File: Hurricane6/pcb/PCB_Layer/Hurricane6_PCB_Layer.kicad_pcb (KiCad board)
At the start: 2 copper layers, 61.5 x 42.5 mm, 19 parts, among them SW1 SW_1, SW2 SW_2, SW3 SW_3, SW4 SW_4, SW5 SW_5, SW6 SW_6, U1 ProMicro-NoSilk

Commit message: feat: consistency of wiring
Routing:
- net Net-(LED1-Pad2): track 33.8 -> 40.6 mm
- net VCC: track 117.3 -> 114.4 mm
- net Net-(LED3-Pad2): track 35.6 -> 38.4 mm
- net Row0: track 69.5 -> 71.0 mm
- net Col2: track 18.9 -> 20.3 mm
- net Col1: track 13.0 -> 13.5 mm

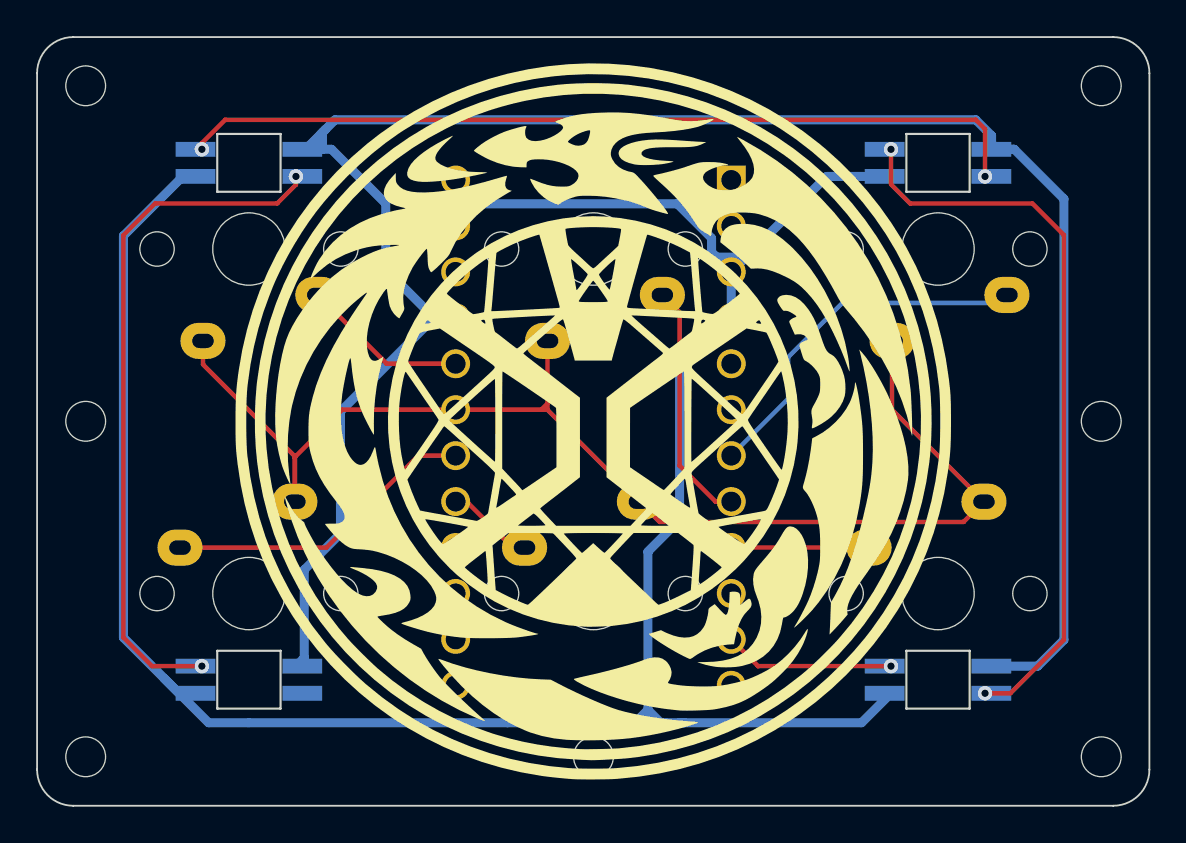
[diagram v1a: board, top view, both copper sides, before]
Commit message: feat: wiring
- consistency of wiring
- remove redundant wiring for GND(pin 3, 23)
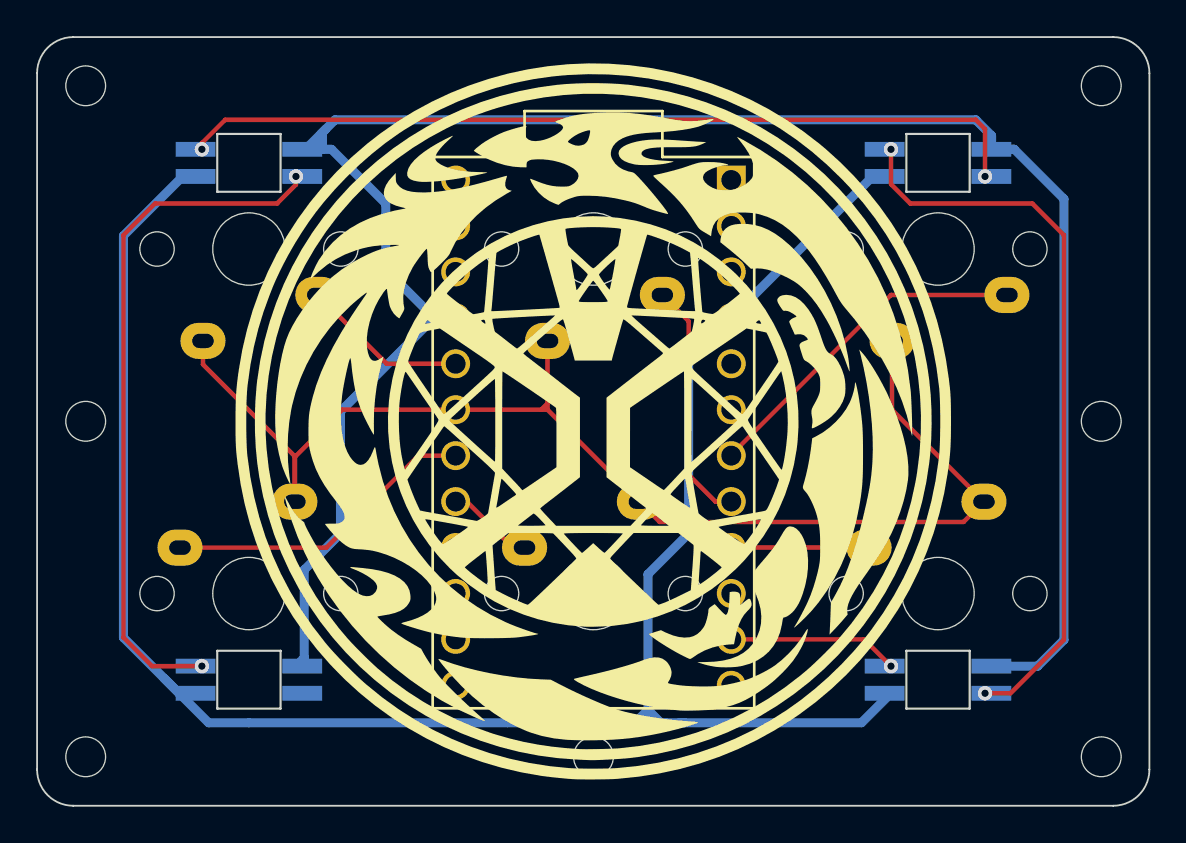
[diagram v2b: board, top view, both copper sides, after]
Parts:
- U1: value ProMicro-NoSilk -> ProMicro; footprint promicro:ProMicro-NoSilk -> promicro:ProMicro
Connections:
- U1 pad 23: GND -> unconnected-(U1-Pad23)
- U1 pad 3: GND -> unconnected-(U1-Pad3)
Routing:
- net GND: track 135.4 -> 114.2 mm
- net Col2: track 20.3 -> 19.6 mm

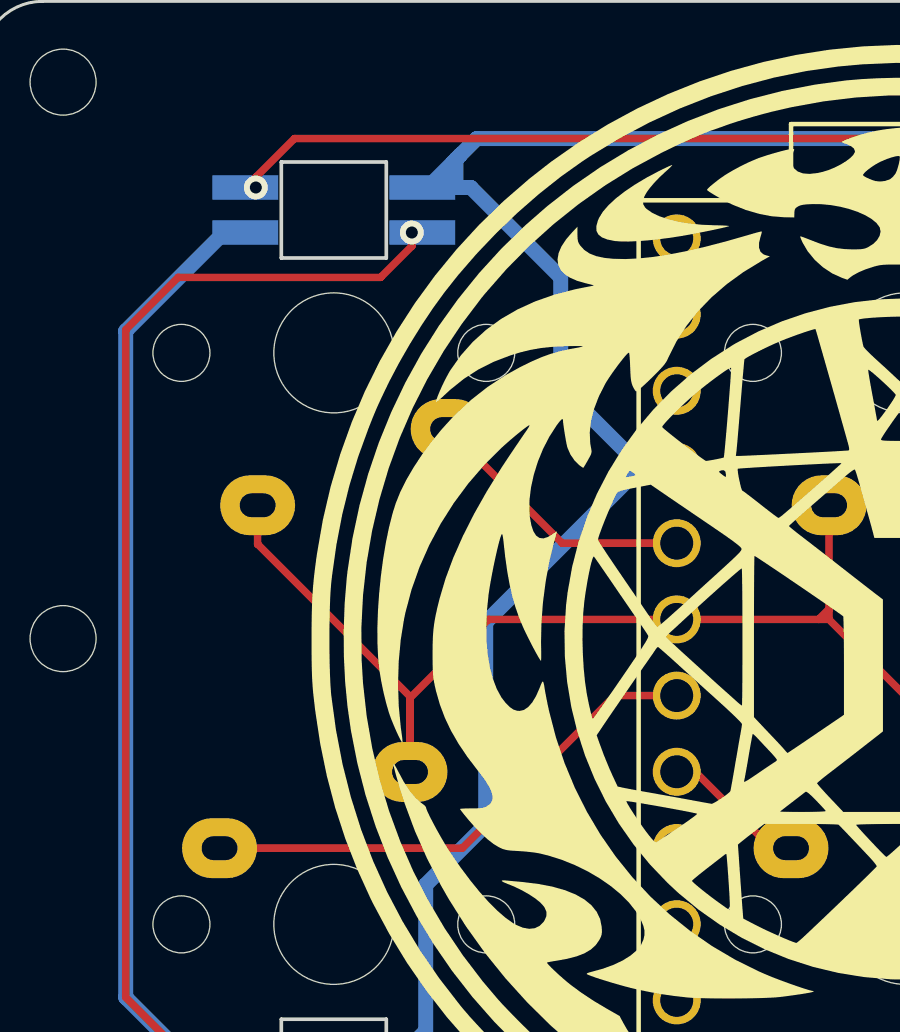
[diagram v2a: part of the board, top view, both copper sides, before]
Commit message: featr: add reset switch and modify wiring
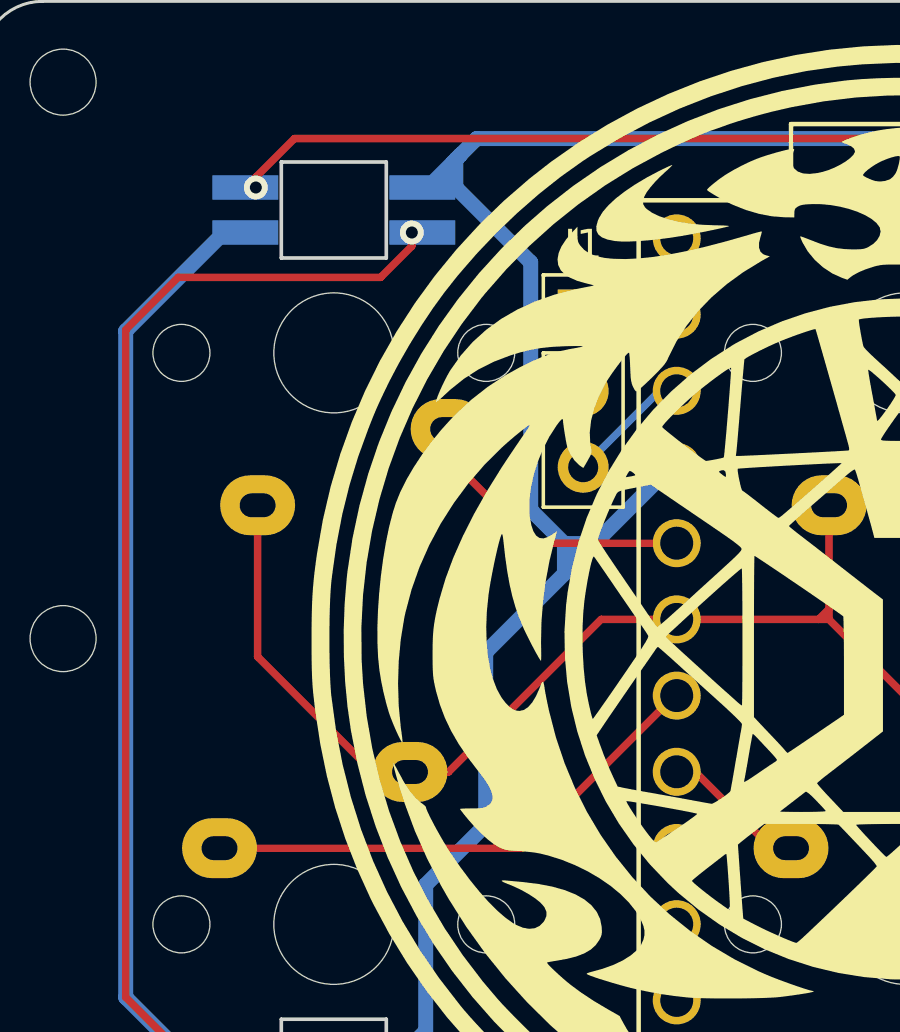
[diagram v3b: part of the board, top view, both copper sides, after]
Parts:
- added J1: Conn_01x03, Connector_PinHeader_2.54mm:PinHeader_1x03_P2.54mm_Vertical, F.Cu at (175.0, 96.2)
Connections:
- U1 pad 22: unconnected-(U1-Pad22) -> Net-(U1-Pad22)
- U1 pad 23: unconnected-(U1-Pad23) -> Net-(U1-Pad23)
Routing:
- net Net-(U1-Pad22): track 0.00 -> 4.20 mm
- net VCC: track 114.4 -> 117.6 mm
- net Net-(U1-Pad23): track 0.00 -> 3.12 mm
- net Row0: track 71.0 -> 70.3 mm
- net Col0: track 9.20 -> 9.75 mm

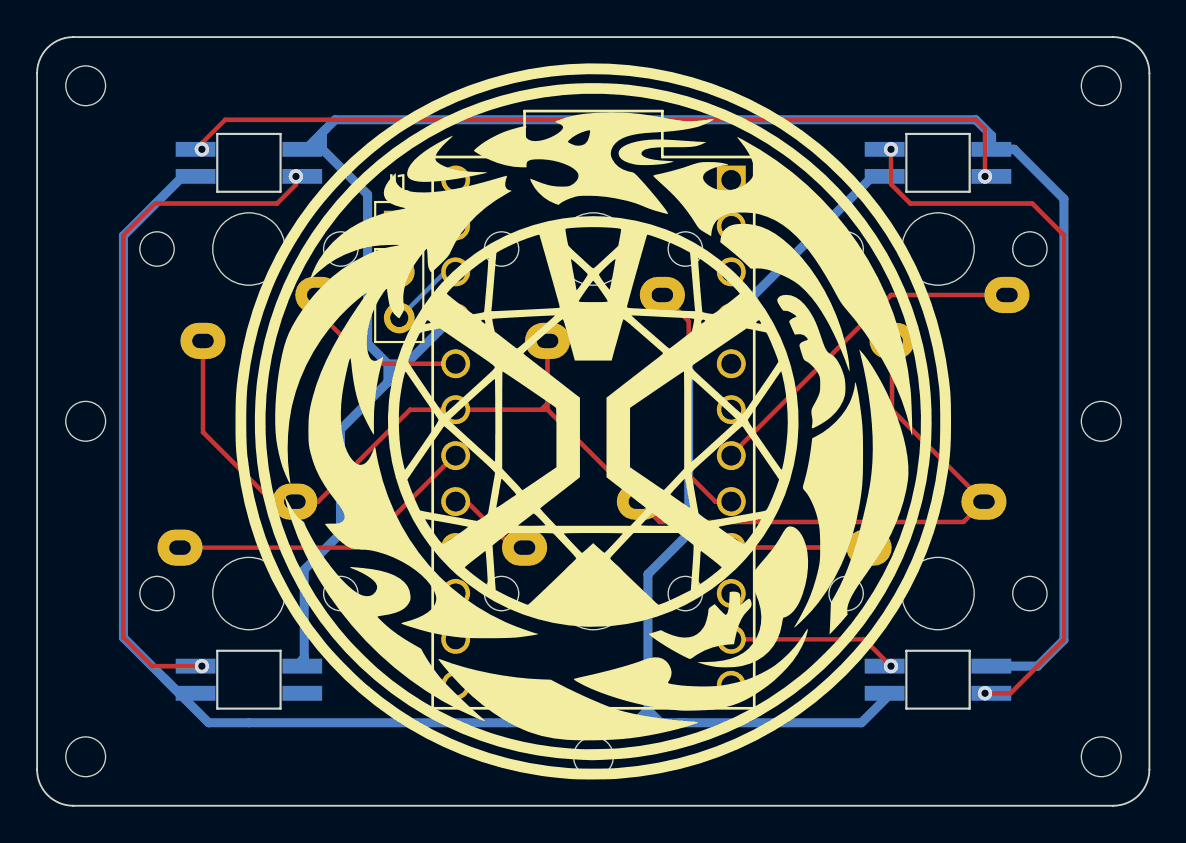
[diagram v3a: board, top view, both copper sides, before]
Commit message: feat: remove logo silk
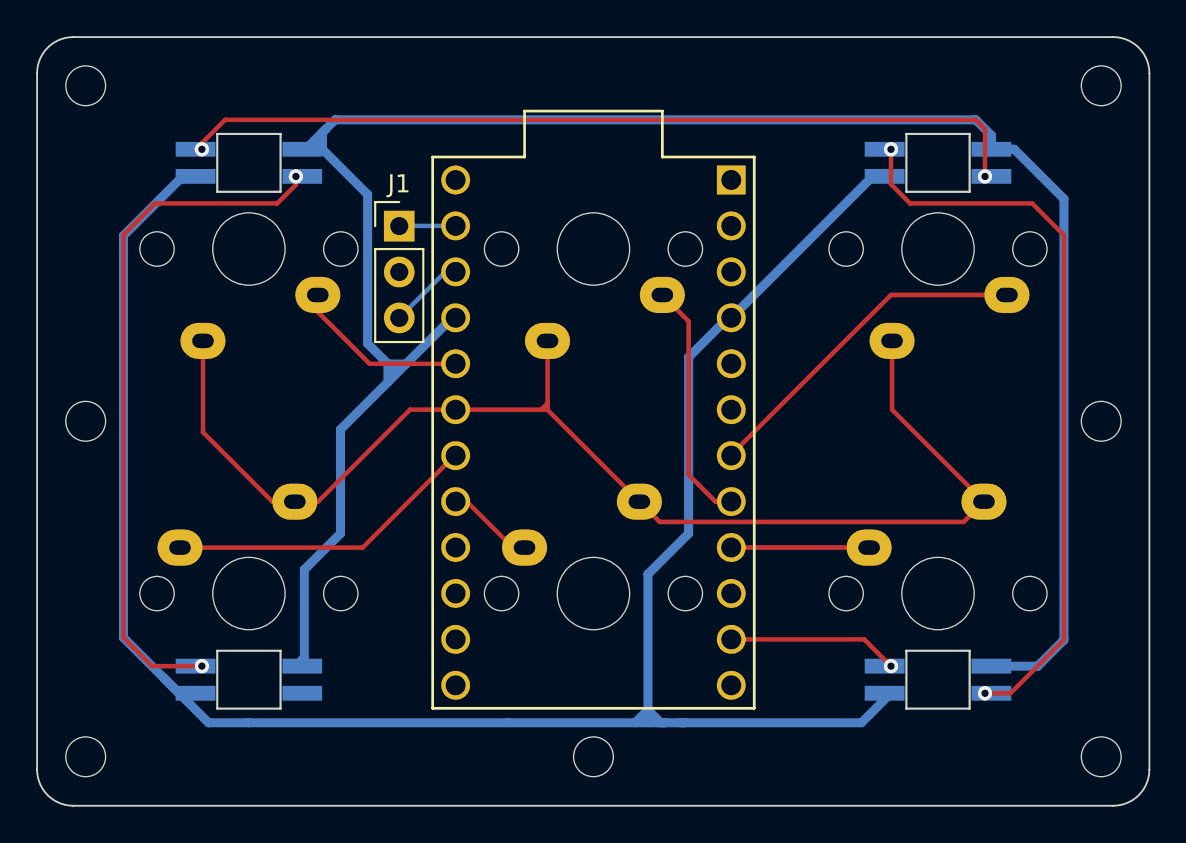
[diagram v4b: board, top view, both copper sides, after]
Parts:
- removed G***: LOGO, Silk_Wizard_logos:silk_wizard_logo_40x40

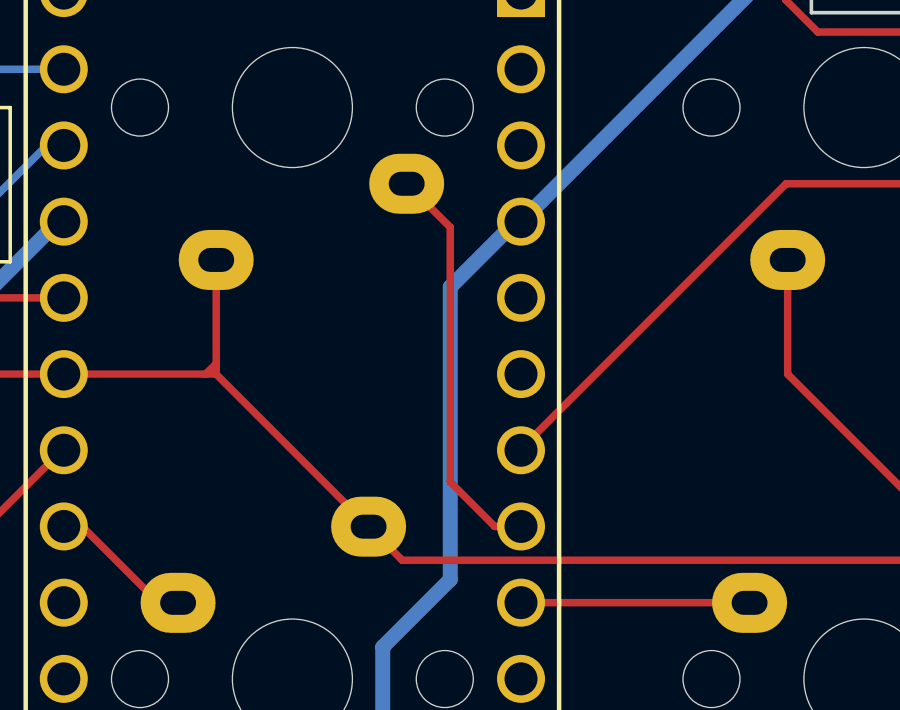
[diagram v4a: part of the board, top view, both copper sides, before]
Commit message: fix: silk text and Y position
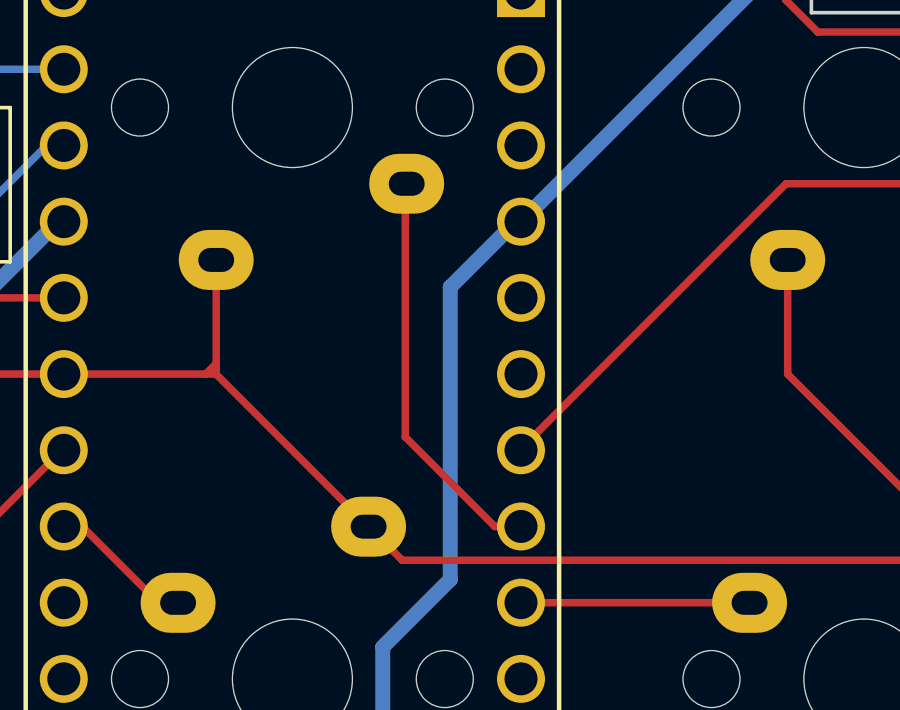
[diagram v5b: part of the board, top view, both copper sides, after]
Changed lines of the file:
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@@
       (drillshape 0)
       (scaleselection 1)
-      (outputdirectory "../../gerber/PCB_Layer1/")
+      (outputdirectory "../../gerber/PCB_Layer/")
     )
   )
@@
   (gr_line (start 214.475 85.8) (end 156.975 85.8) (layer "Edge.Cuts") (width 0.1))
   (gr_arc (start 156.975 128.299986) (mid 155.560784 127.714202) (end 154.975 126.299986) (layer "Edge.Cuts") (width 0.1))
-  (gr_text "Hurricane6 ver1.0 @PCB\nDesigned by multifeb13" (at 161 125.5) (layer "B.SilkS")
+  (gr_text "Hurricane6 ver1.0 @PCB\nDesigned by multifeb13" (at 161 125.592893) (layer "B.SilkS")
     (effects (font (size 1 1) (thickness 0.125)) (justify right mirror))
   )
@@
   (segment (start 178.1175 103.861644) (end 173.361644 103.861644) (width 0.25) (layer "F.Cu") (net 6))
   (segment (start 170.4975 100.9975) (end 170.4975 100.057893) (width 0.25) (layer "F.Cu") (net 6))
-  (segment (start 189.5475 100.057893) (end 191 101.510393) (width 0.25) (layer "F.Cu") (net 7))
-  (segment (start 191 110) (end 192.481644 111.481644) (width 0.25) (layer "F.Cu") (net 7))
+  (segment (start 193.351251 111.487893) (end 193.3575 111.481644) (width 0.25) (layer "F.Cu") (net 7))
+  (segment (start 189.5 108.5) (end 192.481644 111.481644) (width 0.25) (layer "F.Cu") (net 7))
+  (segment (start 189.5 100.105393) (end 189.5 108.5) (width 0.25) (layer "F.Cu") (net 7))
   (segment (start 192.481644 111.481644) (end 193.3575 111.481644) (width 0.25) (layer "F.Cu") (net 7))
-  (segment (start 193.351251 111.487893) (end 193.3575 111.481644) (width 0.25) (layer "F.Cu") (net 7))
-  (segment (start 191 101.510393) (end 191 110) (width 0.25) (layer "F.Cu") (net 7))
+  (segment (start 189.5475 100.057893) (end 189.5 100.105393) (width 0.25) (layer "F.Cu") (net 7))
   (segment (start 193.3575 108.8925) (end 193.3575 108.941644) (width 0.25) (layer "F.Cu") (net 8))
   (segment (start 202.192107 100.057893) (end 193.3575 108.8925) (width 0.25) (layer "F.Cu") (net 8))
